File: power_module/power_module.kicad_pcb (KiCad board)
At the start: 2 copper layers, 29 x 33 mm, 20 parts, among them J1 XT60PW-M, J2 XT60U-M, J3 JST-XH, J4 JST-XH, J5 Conn_01x06, U1 NCV51460, U2 ACS781xLRTR-100U

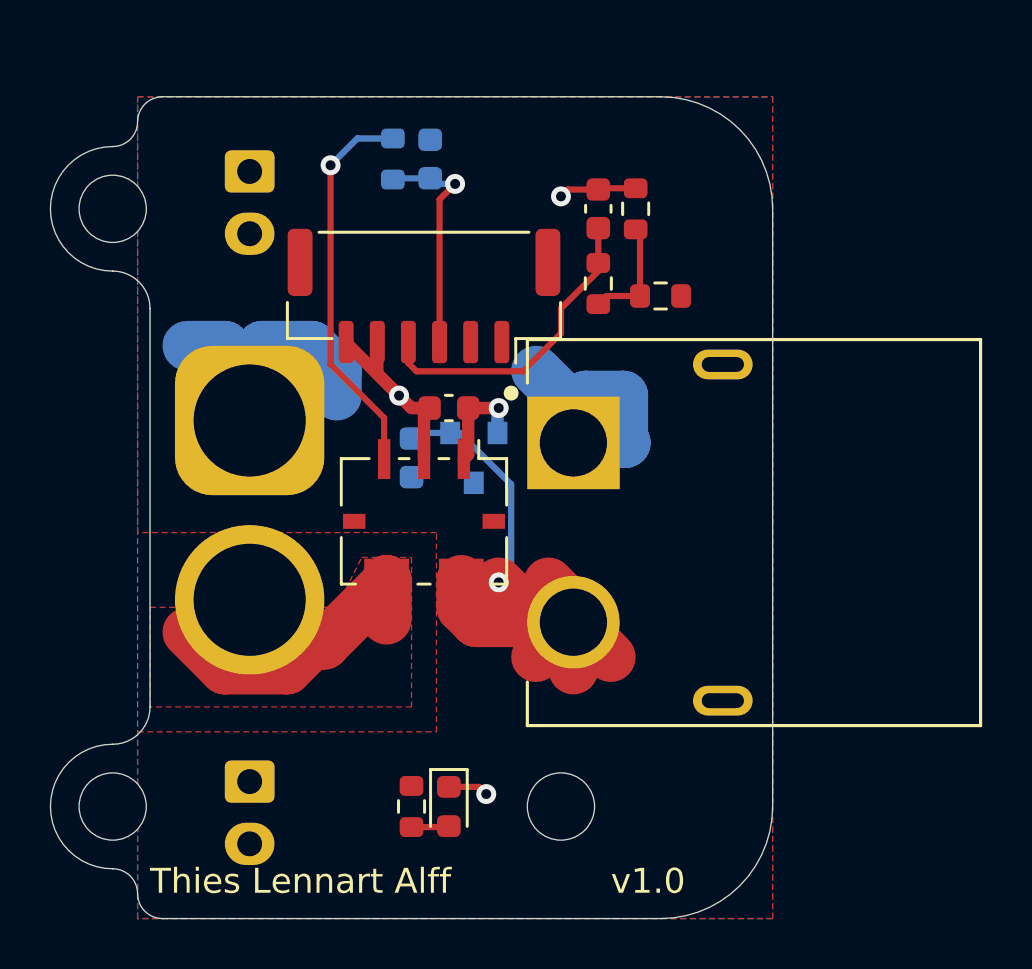
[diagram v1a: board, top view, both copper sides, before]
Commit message: moved battery connector to have a safety margin
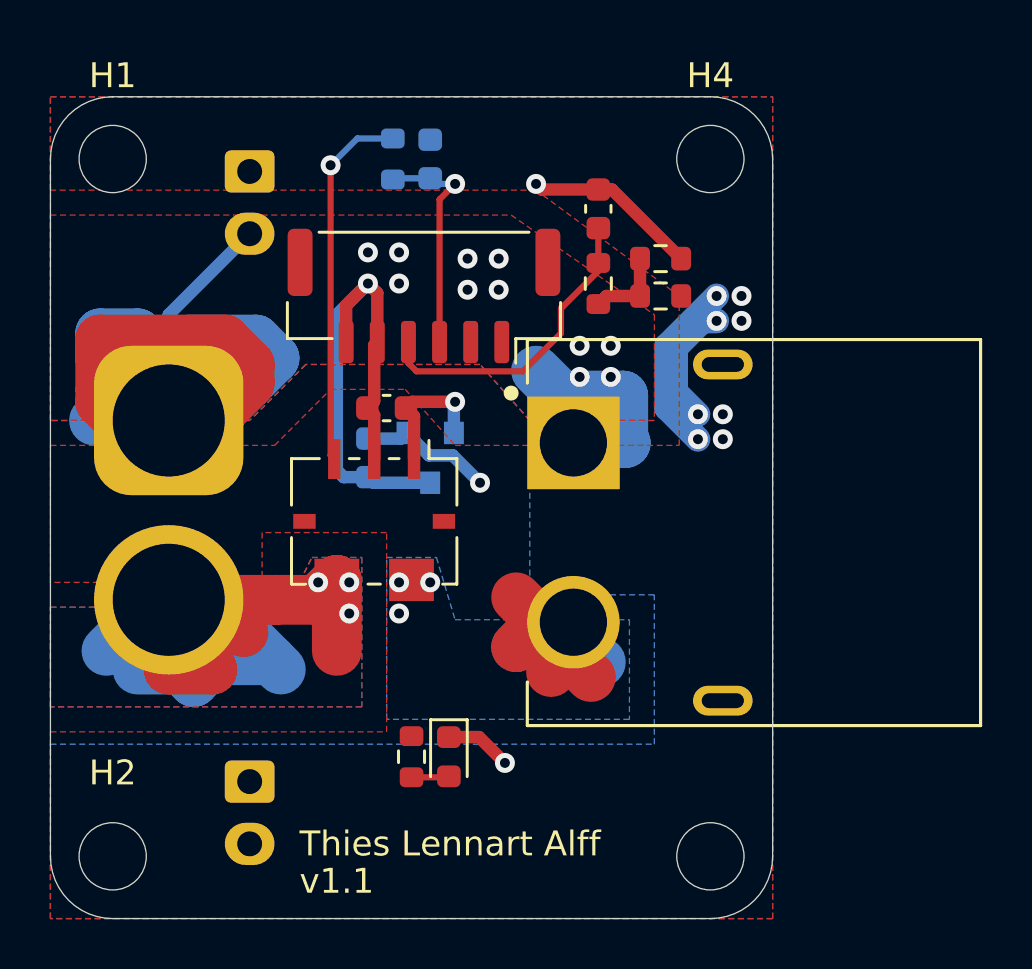
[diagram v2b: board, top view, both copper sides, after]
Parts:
- added H4: MountingHole, hippo:MountingHole_2.7mm_M2.5_Masked, F.Cu at (53.0, 56.0)
- moved H3 6.32 mm to (53.0, 84.0)
- moved J2 3.25 mm to (31.2, 66.5)
- moved C2 2.50 mm to (40.0, 66.0)
- moved R5 2.24 mm to (51.0, 60.0), turned to 0 degrees
- moved D1 2.00 mm to (42.5, 80.0)
- moved H1 2.00 mm to (29.0, 56.0)
- moved H2 2.00 mm to (29.0, 84.0)
- moved R1 2.00 mm to (41.0, 80.0)
- moved U2 2.00 mm to (39.5, 70.5)
- moved C1 1.75 mm to (39.2, 68.0)
- moved U1 1.75 mm to (41.8, 68.0)
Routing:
- net GND: track 34.8 -> 85.9 mm, vias 3 -> 14
- net /+BATT_RAW: track 11.8 -> 41.6 mm, vias 0 -> 3
- net +BATT: track 26.7 -> 34.1 mm, vias 1 -> 12
- net Net-(R3-Pad1): track 4.56 -> 3.31 mm
- net +3V3: track 4.37 -> 5.53 mm
- added copper zone on B.Cu, net +BATT
- added copper zone on B.Cu, net /+BATT_RAW
- added copper zone on F.Cu, net GND
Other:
- outline, holes or cut-outs redrawn
- board text added: "v1.1"
- board text removed: "v1.0"
